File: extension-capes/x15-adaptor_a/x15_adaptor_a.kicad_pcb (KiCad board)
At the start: 2 copper layers, 39 x 46 mm, 67 parts, among them P1 FX18-60S-0.8SV15, P2 I2S, P3 SPI

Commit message: x15 adaptor production stage
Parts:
- added G***: LOGO, modules:cc-logo, B.Cu at (142.2, 92.5)
- P2, P3, T1, T10, T11, T12, T12V0, T13, T14, T15, T16, T17, T18, T19, T2, T20, T21, T22, T23, T24, T25, T26, T27, T28, T29, T3, T30, T31, T32, T33, T34, T35, T36, T37, T38, T39, T3V3, T4, T40, T41, T42, T43, T44, T45, T46, T47, T48, T49, T5, T50, T51, T52, T53, T54, T55, T56, T57, T58, T59, T5V0, T6, T60, T7, T8, T9, TGND0: moved to B.Cu
- moved P2 48.3 mm to (165.5, 49.1), turned to 90 degrees
- moved P3 46.8 mm to (165.5, 92.2), turned to 90 degrees
- moved T33 45.8 mm to (161.4, 54.9)
- moved T36 45.7 mm to (158.8, 54.9)
- moved T39 45.6 mm to (156.3, 54.9)
- moved T42 45.4 mm to (153.7, 54.9)
- moved T1 45.4 mm to (163.0, 79.5)
- moved T45 45.3 mm to (151.2, 54.9)
- moved T4 45.3 mm to (160.4, 79.5)
- moved T48 45.2 mm to (148.7, 54.9)
- moved T7 45.2 mm to (157.9, 79.5)
- moved P1 45.2 mm to (163.0, 71.1)
- moved T51 45.1 mm to (146.1, 54.9)
- moved T3V3 45.1 mm to (135.0, 63.5)
- moved T32 45.1 mm to (162.2, 59.2)
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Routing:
- net /ASDATA1: track 28.0 -> 40.5 mm
- net /ALRCLK: track 27.9 -> 38.3 mm, vias 0 -> 1
- net /3V3: track 59.2 -> 69.1 mm
- net GND: track 56.3 -> 64.0 mm
- net /DLRCLK: track 18.2 -> 23.7 mm
- net /DSDATA1: track 37.0 -> 40.7 mm
- net /RESET: track 44.8 -> 48.0 mm
- net /ABCLK: track 17.5 -> 20.6 mm
- net /SPI_CS: track 24.8 -> 22.0 mm
- net /SPI_DO: track 36.4 -> 38.9 mm
- net /DBCLK: track 37.6 -> 39.8 mm
- net Net-(P1-Pad27): track 12.3 -> 14.1 mm
- net Net-(P1-Pad24): track 12.3 -> 14.1 mm
- net Net-(P1-Pad60): track 12.2 -> 13.8 mm
- net Net-(P1-Pad15): track 12.3 -> 13.9 mm
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- added copper zone on B.Cu, net GND
- added copper zone on F.Cu, net GND
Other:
- board size 39 x 46 mm -> 38 x 49.5 mm
- rule pad_to_mask_clearance: 0.2 -> 0.0381
- board text added: "(c) R. Manzke 2016"
- board text added: "CTAG X15 Breakout Brd. Rev. A www.creative-technologies.de"

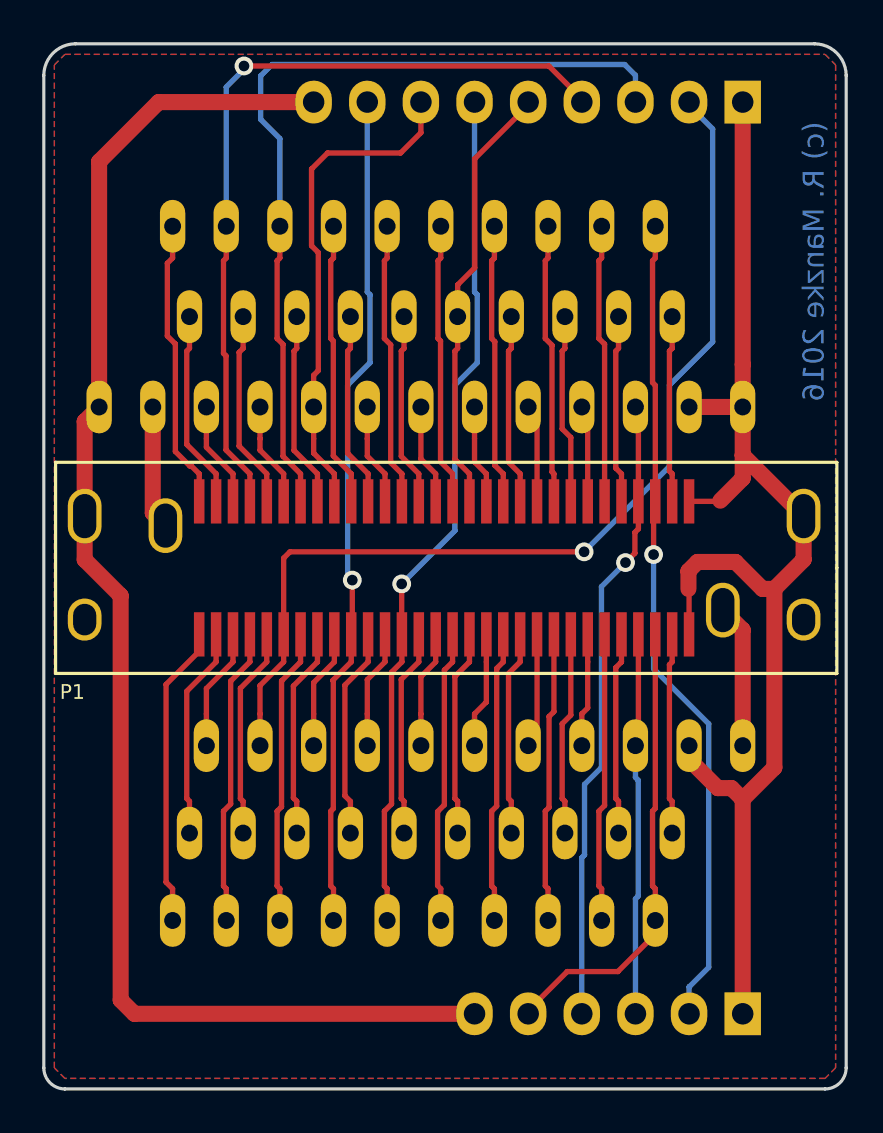
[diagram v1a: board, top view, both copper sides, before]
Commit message: changed diameters of test pin holes
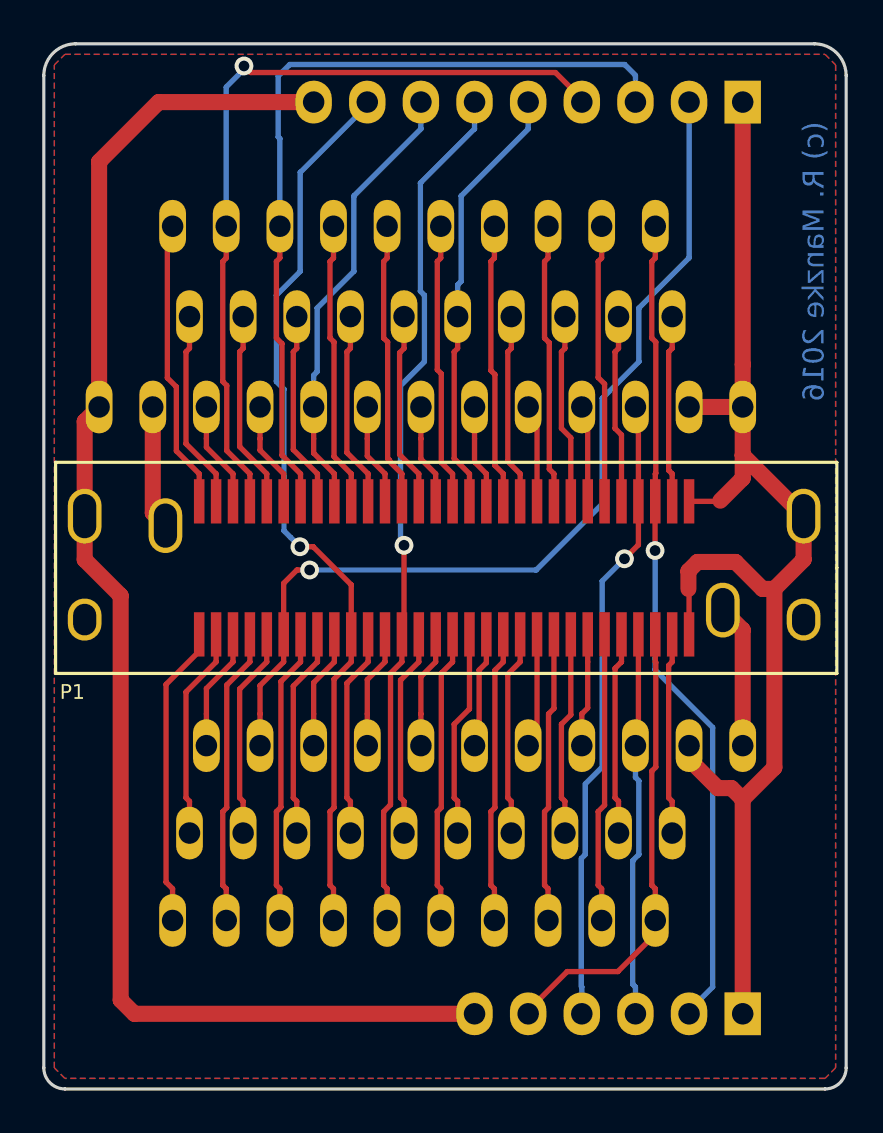
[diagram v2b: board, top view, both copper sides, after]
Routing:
- net /DBCLK: track 39.8 -> 42.9 mm
- net /RESET: track 48.0 -> 45.7 mm
- net /DLRCLK: track 23.7 -> 21.4 mm
- net /ASDATA1: track 40.5 -> 39.3 mm

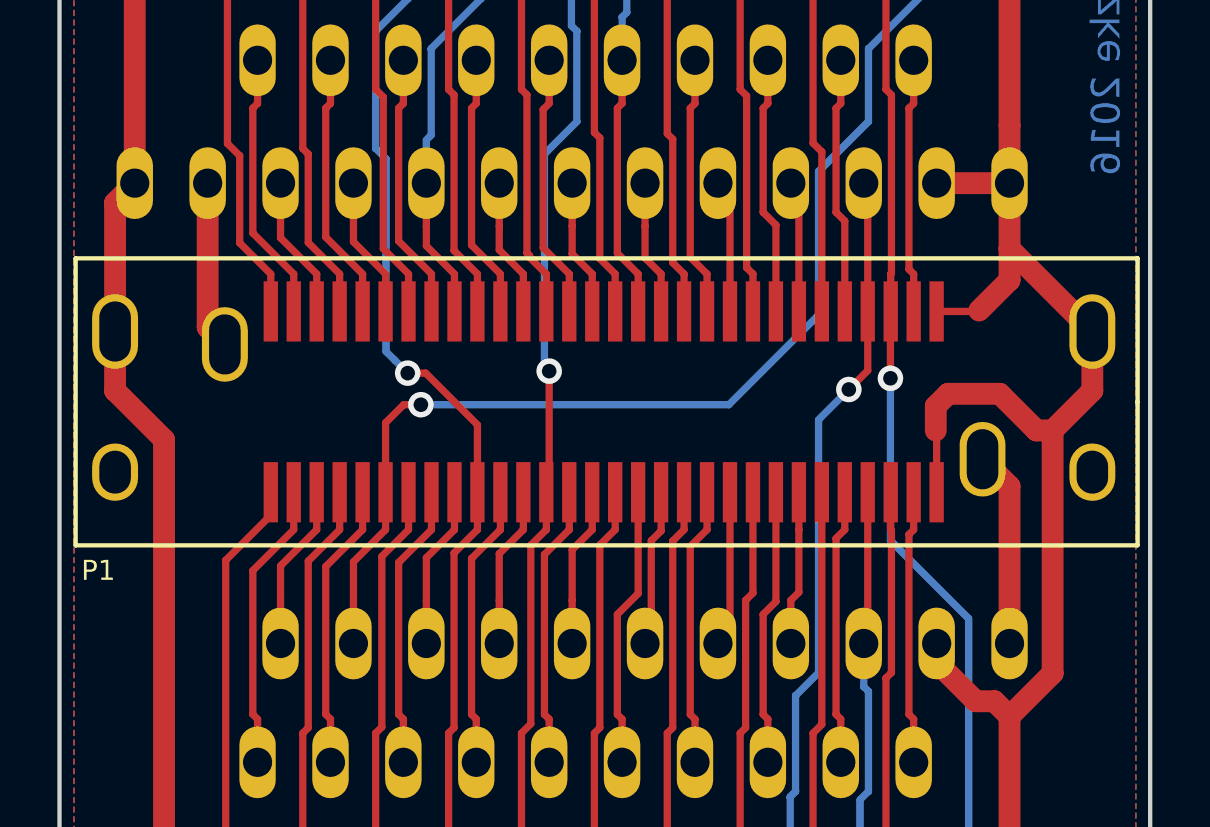
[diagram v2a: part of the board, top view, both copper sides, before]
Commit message: added multiple holes for oblong shape to account for boardhouse capabilities
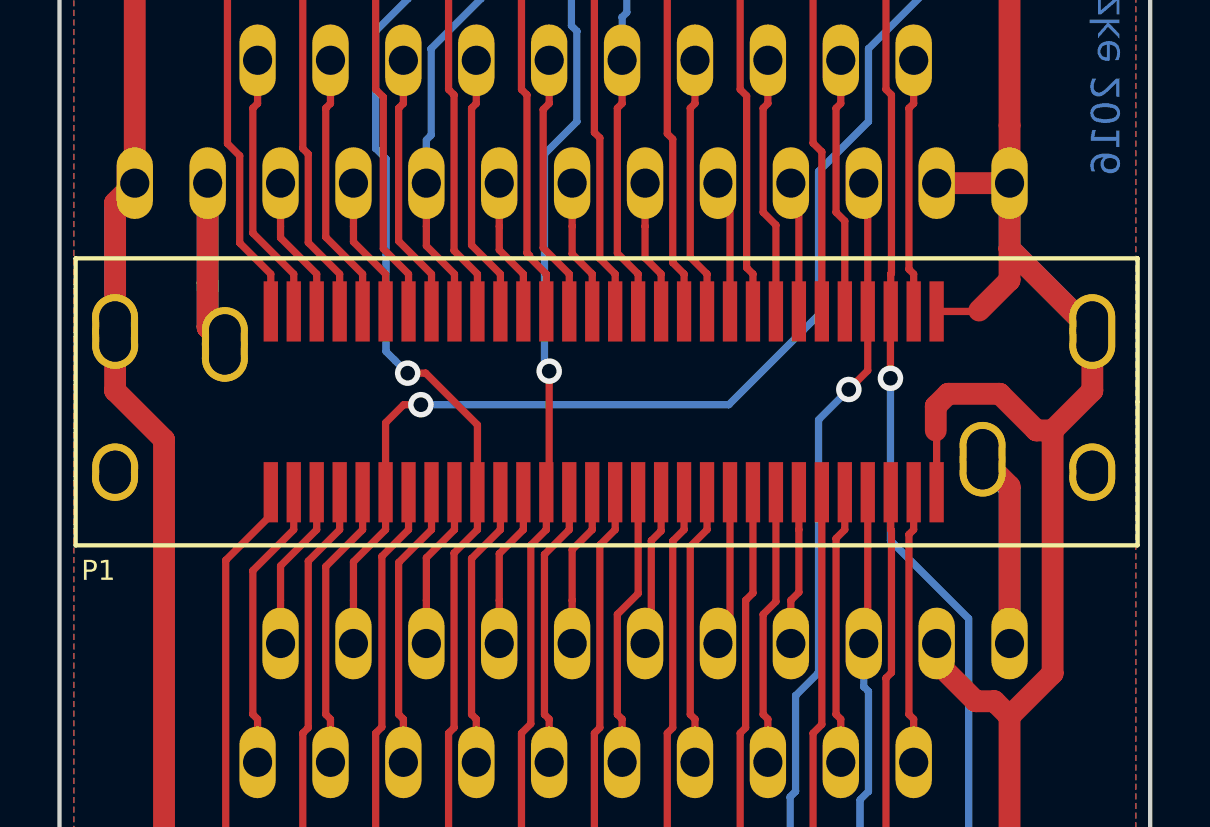
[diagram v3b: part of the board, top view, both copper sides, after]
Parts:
- added REF**: Extrapad, HiroseFX:Extrapad, F.Cu at (168.4, 73.4)
- added REF**: Extrapad, HiroseFX:Extrapad, F.Cu at (138.2, 69.6)
- added REF**: Extrapad, HiroseFX:Extrapad, F.Cu at (138.2, 69.1)
- added REF**: Extrapad, HiroseFX:Extrapad, F.Cu at (134.3, 68.2)
- added REF**: Extrapad, HiroseFX:Extrapad, F.Cu at (134.3, 69.2)
- added REF**: Extrapad, HiroseFX:Extrapad, F.Cu at (134.3, 68.7)
- added REF**: Extrapad, HiroseFX:Extrapad, F.Cu at (134.3, 73.4)
- added REF**: Extrapad, HiroseFX:Extrapad, F.Cu at (134.3, 73.8)
- added REF**: Extrapad, HiroseFX:Extrapad, F.Cu at (168.4, 73.8)
- added REF**: Extrapad, HiroseFX:Extrapad, F.Cu at (168.4, 68.2)
- added REF**: Extrapad, HiroseFX:Extrapad, F.Cu at (168.4, 69.2)
- added REF**: Extrapad, HiroseFX:Extrapad, F.Cu at (168.4, 68.6)
- added REF**: Extrapad, HiroseFX:Extrapad, F.Cu at (164.6, 72.6)
- added REF**: Extrapad, HiroseFX:Extrapad, F.Cu at (164.6, 73.6)
- added REF**: Extrapad, HiroseFX:Extrapad, F.Cu at (164.6, 73.1)
- added REF**: Extrapad, HiroseFX:Extrapad, F.Cu at (138.2, 68.6)
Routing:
- net /5V0: track 5.87 -> 13.7 mm
- net /12V0: track 6.81 -> 13.6 mm
- net GND: track 64.0 -> 70.3 mm
- net /3V3: track 69.1 -> 74.5 mm
